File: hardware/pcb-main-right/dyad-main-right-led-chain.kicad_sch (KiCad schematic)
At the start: 74 parts

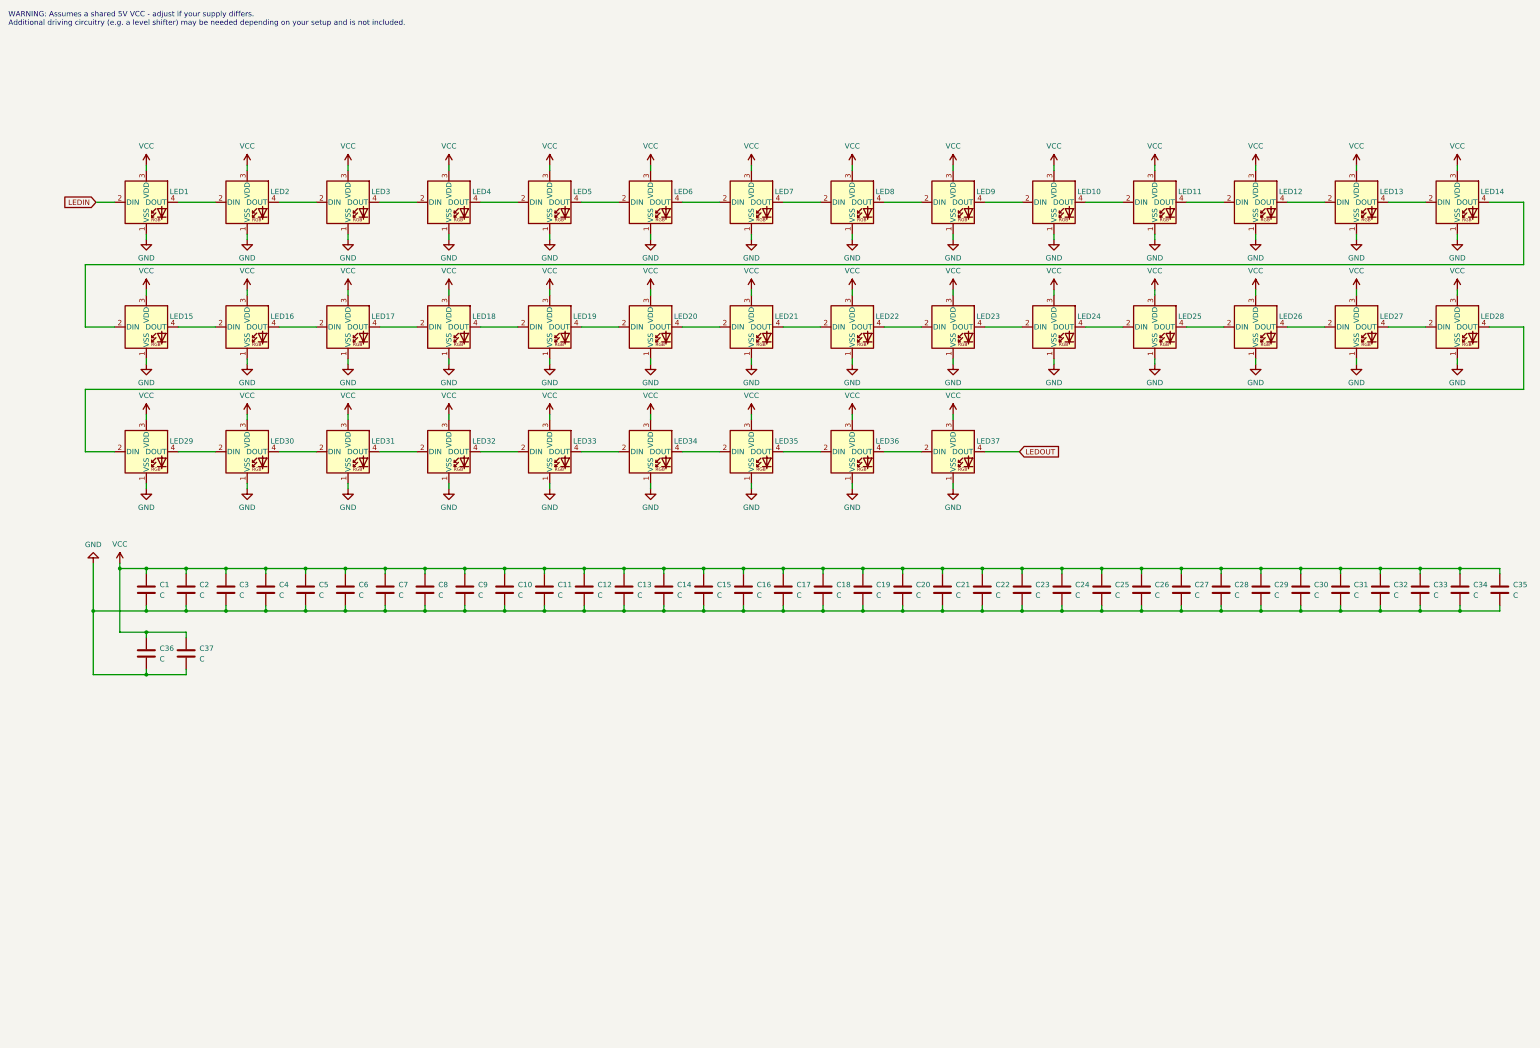
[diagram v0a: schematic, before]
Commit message: Restore the hand-drawn serpentine LED chain for the right half
I regenerated the right half without checking whether its schematics held
work that was not yet committed, and overwrote a hand-laid serpentine LED
chain. Recovered from hardware/pcb-main-right/.history, KiCad's own version
history repo, at its "SCH Save" commit a7ba379 (2026-09-15 12:59).

The led-chain sheet is byte-identical to that save: 74 symbols, 16 of them
rotated 180 degrees for the alternating rows, with every symbol repositioned
into serpentine order. All 272 wires differ from the generated version, so
this was a full re-layout rather than a rewire.

That history commit happens to postdate 2826d7a, so the bottom-row column
remap and both copper pours came back with it. The only thing missing was
the footprint linking from 2acfb55, re-applied here by calling
_link_footprints_to_symbols directly -- no kbplacer run, so nothing was
regenerated. 148/148 footprints linked.

The board still carries the old sequential chain, which is what the 31
parity findings say:

  Pad net (Net-(LEDn-DOUT)) doesn't match net given by schematic
  (Net-(LEDn-DIN))

That is the serpentine waiting to be pushed with Update PCB from Schematic,
which the footprint links now make possible. The 7 clearance and 7
solder_mask_bridge errors come from the same divergence and should go with it.

Co-Authored-By: Claude Opus 5 <noreply@anthropic.com>
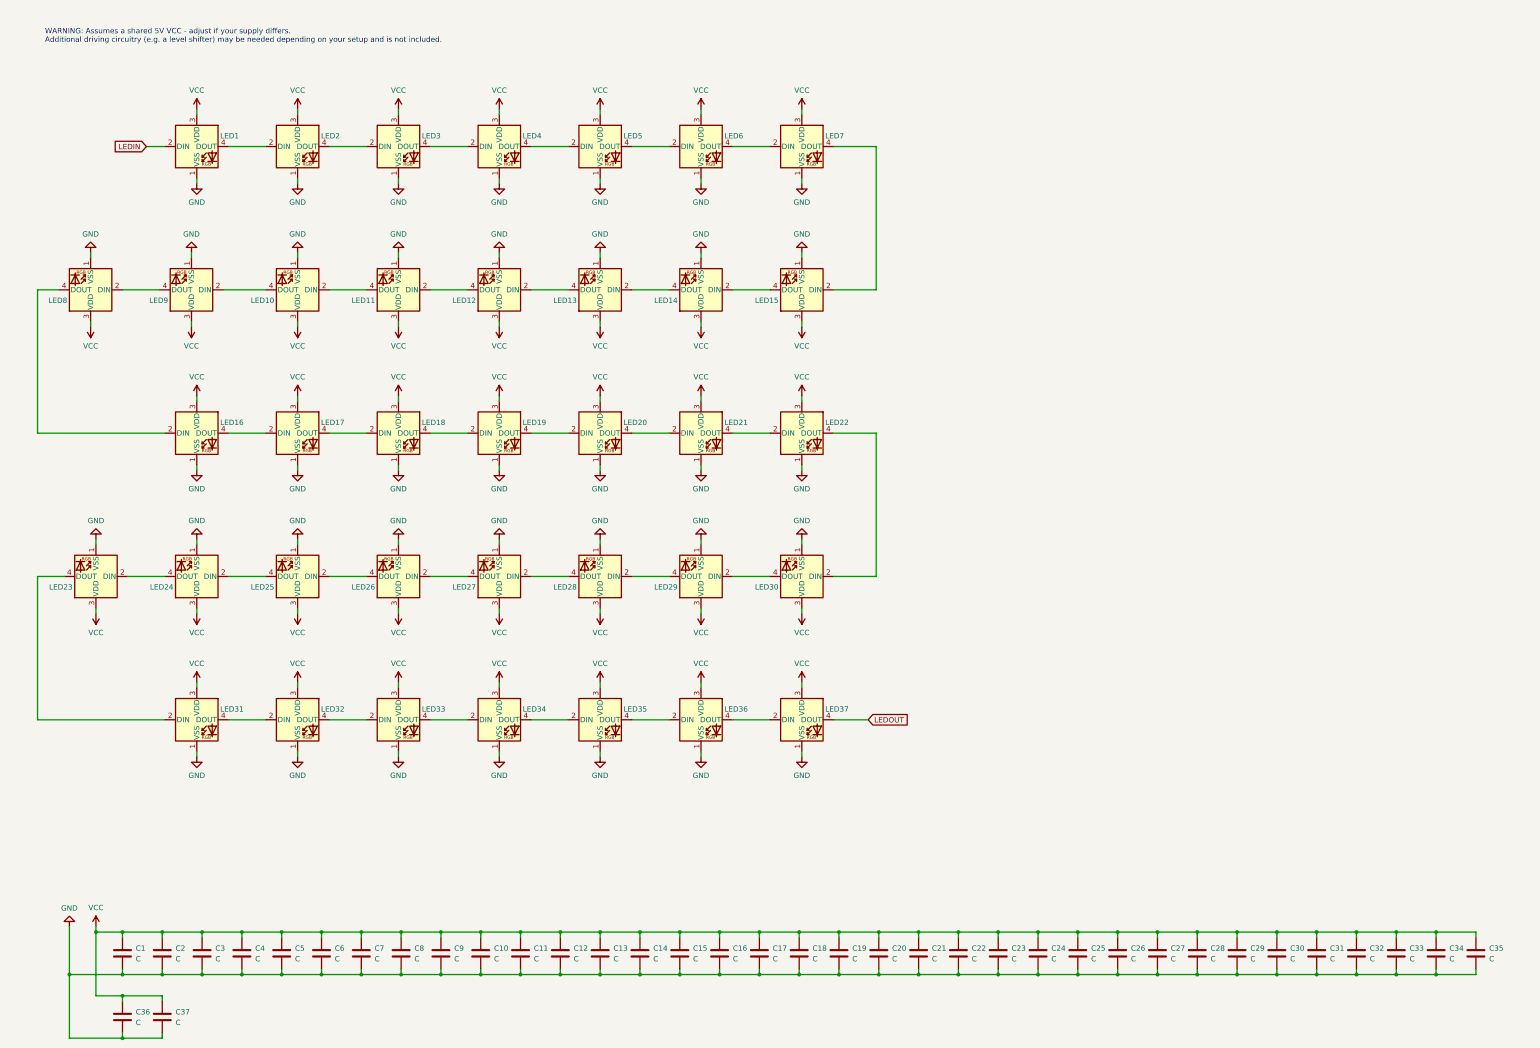
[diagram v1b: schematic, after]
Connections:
- net at LED12.4 (DOUT): now also LED11.2 (DIN); no longer LED13.2 (DIN)
- net at LED13.4 (DOUT): now also LED12.2 (DIN); no longer LED14.2 (DIN)
- net at LED23.2 (DIN): now also LED24.4 (DOUT); no longer LED22.4 (DOUT)
- net at LED24.2 (DIN): now also LED25.4 (DOUT); no longer LED23.4 (DOUT)
- net at LED15.4 (DOUT): now also LED14.2 (DIN); no longer LED16.2 (DIN)
- net at LED7.4 (DOUT): now also LED15.2 (DIN); no longer LED8.2 (DIN)
- net at LED9.2 (DIN): now also LED10.4 (DOUT); no longer LED8.4 (DOUT)
- net at LED10.2 (DIN): now also LED11.4 (DOUT); no longer LED9.4 (DOUT)
- net at LED14.4 (DOUT): now also LED13.2 (DIN); no longer LED15.2 (DIN)
- net at LED26.2 (DIN): now also LED27.4 (DOUT); no longer LED25.4 (DOUT)
- net at LED27.2 (DIN): now also LED28.4 (DOUT); no longer LED26.4 (DOUT)
- net at LED29.2 (DIN): now also LED30.4 (DOUT); no longer LED28.4 (DOUT)
- net at LED29.4 (DOUT): now also LED28.2 (DIN); no longer LED30.2 (DIN)
- net at LED25.2 (DIN): now also LED26.4 (DOUT); no longer LED24.4 (DOUT)
- net at LED31.2 (DIN): now also LED23.4 (DOUT); no longer LED30.4 (DOUT)
- new net: LED22.4 (DOUT), LED30.2 (DIN)
- new net: LED16.2 (DIN), LED8.4 (DOUT)
- new net: LED8.2 (DIN), LED9.4 (DOUT)
